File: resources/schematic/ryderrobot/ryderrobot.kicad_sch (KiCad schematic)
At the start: 14 parts, among them U1 HC-SR04, U2 HC-SR04, U3 HC-SR04

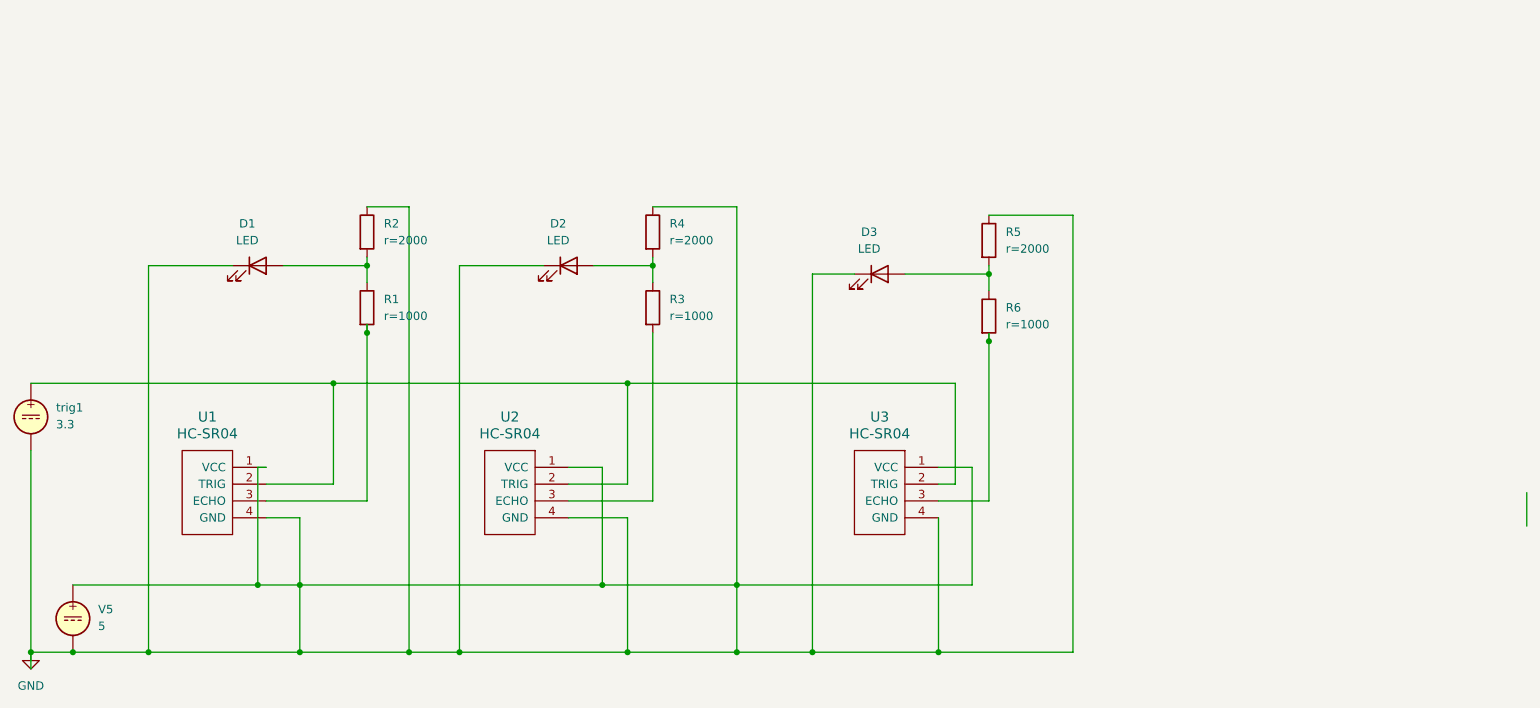
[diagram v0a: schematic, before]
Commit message: updated README and some testing on schematic
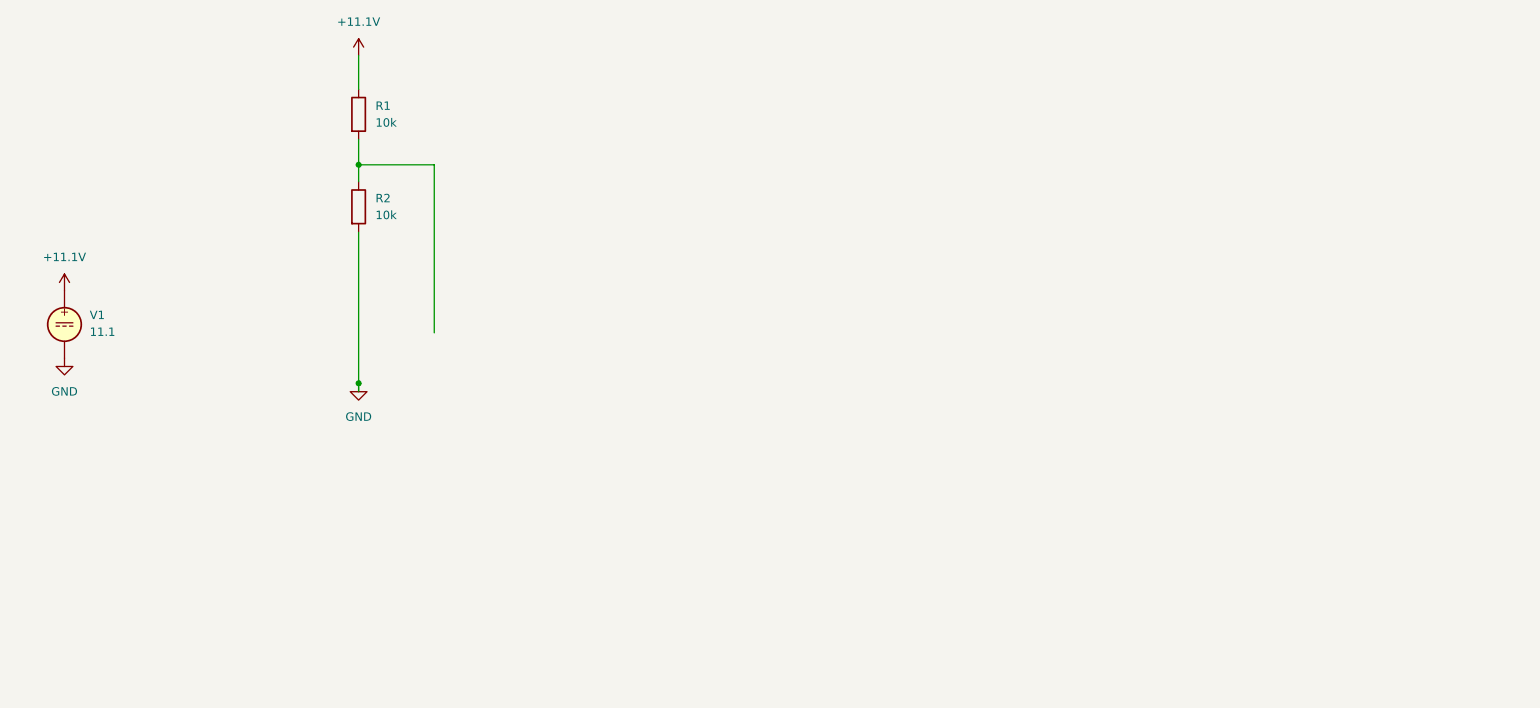
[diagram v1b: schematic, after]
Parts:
- removed D1, D2, D3: LED, symbol Device:LED
- removed R3, R4, R5, R6: ${SIM.PARAMS}, symbol Device:R
- removed U1, U2, U3: HC-SR04, symbol hc-sr04:HC-SR04
- removed V5: 5, symbol Simulation_SPICE:VDC
- removed trig1: 3.3, symbol Simulation_SPICE:VDC
- added V1: 11.1, symbol Simulation_SPICE:VDC
- R1, R2: value ${SIM.PARAMS} -> 10k
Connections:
- net GND: now also R2.2, V1.2; no longer R2.1
- net +11.1V: now reaches R1.1
- net +11.1V: now also V1.1; no longer R2.2
- net at R1.2: now also R2.1
